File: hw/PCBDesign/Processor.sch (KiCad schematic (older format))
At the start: 26 parts, among them J4 Conn_ARM_JTAG_SWD_10, U11 74HC595, U12 74HC595, U13 STM32F446RETx, Y1 8MHz Crystal

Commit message: Lay out more PCB
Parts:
- added C29, C31, C33, C55, C56, C57: 100n, Capacitor_SMD:C_0402_1005Metric, symbol Device:C
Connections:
- net labels removed: BT_IRQ, BT_nPowerUp, BT_nWakeup, VSense_Analog, VSense_Radio, vBatt_Sense
- no-connect marks 6 -> 15
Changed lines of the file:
@@
 Text HLabel 8100 5700 2    50   Input ~ 0
 nBatt_Chg_Good
-Text HLabel 8800 1400 2    50   Input ~ 0
-vBatt_Sense
-Text HLabel 3350 2100 2    50   Output ~ 0
+Text HLabel 3550 2100 2    50   Output ~ 0
 nBattChgEn
-Text HLabel 3350 1900 2    50   Output ~ 0
+Text HLabel 3550 1900 2    50   Output ~ 0
 BattChgCfg0
-Text HLabel 3350 2000 2    50   Output ~ 0
+Text HLabel 3550 2000 2    50   Output ~ 0
 BattChgCfg1
 Text HLabel 7400 3700 0    50   Input ~ 0
@@
 Text HLabel 7400 3600 0    50   Output ~ 0
 BT_UART_TX
-Text HLabel 3350 2200 2    50   Output ~ 0
-BT_nWakeup
-Text HLabel 3350 2300 2    50   Output ~ 0
-BT_nPowerUp
-Text HLabel 7400 3800 0    50   Input ~ 0
-BT_IRQ
 Text HLabel 8800 2100 2    50   Output ~ 0
 RF24_MOSI
@@
 Text HLabel 8800 1500 2    50   Input ~ 0
 VSense_Digital
-Text HLabel 8800 1600 2    50   Input ~ 0
-VSense_Radio
-Text HLabel 8800 1700 2    50   Input ~ 0
-VSense_Analog
 Text HLabel 8100 1100 1    50   Input ~ 0
 V+
@@
 	6850 2700 6850 2600
 Connection ~ 6400 2700
-Text HLabel 3350 2400 2    50   Output ~ 0
+Text HLabel 3550 2400 2    50   Output ~ 0
 BT_VCC_EN
-Text HLabel 3350 2500 2    50   Output ~ 0
+Text HLabel 3550 2500 2    50   Output ~ 0
 RF24_VCC_EN
 Text Notes 3800 5600 0    50   ~ 0
@@
 Wire Wire Line
 	9400 2500 8800 2500
+NoConn ~ 7400 4300
+NoConn ~ 7400 4400
+NoConn ~ 7400 4500
+NoConn ~ 8800 3800
+NoConn ~ 8800 3300
+$Comp
+L Device:C C55
+U 1 1 6065388D
+P 5500 1300
+F 0 "C55" H 5615 1346 50  0000 L CNN
+F 1 "100n" H 5615 1255 50  0000 L CNN
+F 2 "Capacitor_SMD:C_0402_1005Metric" H 5538 1150 50  0001 C CNN
+F 3 "~" H 5500 1300 50  0001 C CNN
+F 4 "C1525" H 5500 1300 50  0001 C CNN "LCSC"
+	1    5500 1300
+	1    0    0    -1
+$EndComp
+$Comp
+L Device:C C56
+U 1 1 606541DA
+P 5900 1300
+F 0 "C56" H 6015 1346 50  0000 L CNN
+F 1 "100n" H 6015 1255 50  0000 L CNN
+F 2 "Capacitor_SMD:C_0402_1005Metric" H 5938 1150 50  0001 C CNN
+F 3 "~" H 5900 1300 50  0001 C CNN
+F 4 "C1525" H 5900 1300 50  0001 C CNN "LCSC"
+	1    5900 1300
+	1    0    0    -1
+$EndComp
+$Comp
+L Device:C C57
+U 1 1 6065440B
+P 6300 1300
+F 0 "C57" H 6415 1346 50  0000 L CNN
+F 1 "100n" H 6415 1255 50  0000 L CNN
+F 2 "Capacitor_SMD:C_0402_1005Metric" H 6338 1150 50  0001 C CNN
+F 3 "~" H 6300 1300 50  0001 C CNN
+F 4 "C1525" H 6300 1300 50  0001 C CNN "LCSC"
+	1    6300 1300
+	1    0    0    -1
+$EndComp
+$Comp
+L Device:C C33
+U 1 1 60654852
+P 5100 1300
+F 0 "C33" H 5215 1346 50  0000 L CNN
+F 1 "100n" H 5215 1255 50  0000 L CNN
+F 2 "Capacitor_SMD:C_0402_1005Metric" H 5138 1150 50  0001 C CNN
+F 3 "~" H 5100 1300 50  0001 C CNN
+F 4 "C1525" H 5100 1300 50  0001 C CNN "LCSC"
+	1    5100 1300
+	1    0    0    -1
+$EndComp
+$Comp
+L Device:C C31
+U 1 1 60654BAF
+P 4700 1300
+F 0 "C31" H 4815 1346 50  0000 L CNN
+F 1 "100n" H 4815 1255 50  0000 L CNN
+F 2 "Capacitor_SMD:C_0402_1005Metric" H 4738 1150 50  0001 C CNN
+F 3 "~" H 4700 1300 50  0001 C CNN
+F 4 "C1525" H 4700 1300 50  0001 C CNN "LCSC"
+	1    4700 1300
+	1    0    0    -1
+$EndComp
+$Comp
+L Device:C C29
+U 1 1 606550A4
+P 4300 1300
+F 0 "C29" H 4415 1346 50  0000 L CNN
+F 1 "100n" H 4415 1255 50  0000 L CNN
+F 2 "Capacitor_SMD:C_0402_1005Metric" H 4338 1150 50  0001 C CNN
+F 3 "~" H 4300 1300 50  0001 C CNN
+F 4 "C1525" H 4300 1300 50  0001 C CNN "LCSC"
+	1    4300 1300
+	1    0    0    -1
+$EndComp
+Text HLabel 5900 1150 1    50   Input ~ 0
+V+
+Text HLabel 5500 1150 1    50   Input ~ 0
+V+
+Text HLabel 5100 1150 1    50   Input ~ 0
+V+
+Text HLabel 4700 1150 1    50   Input ~ 0
+V+
+Text HLabel 4300 1150 1    50   Input ~ 0
+V+
+$Comp
+L power:GND #PWR0122
+U 1 1 60655583
+P 6300 1450
+F 0 "#PWR0122" H 6300 1200 50  0001 C CNN
+F 1 "GND" H 6305 1277 50  0000 C CNN
+F 2 "" H 6300 1450 50  0001 C CNN
+F 3 "" H 6300 1450 50  0001 C CNN
+	1    6300 1450
+	1    0    0    -1
+$EndComp
+$Comp
+L power:GND #PWR0123
+U 1 1 60655871
+P 5900 1450
+F 0 "#PWR0123" H 5900 1200 50  0001 C CNN
+F 1 "GND" H 5905 1277 50  0000 C CNN
+F 2 "" H 5900 1450 50  0001 C CNN
+F 3 "" H 5900 1450 50  0001 C CNN
+	1    5900 1450
+	1    0    0    -1
+$EndComp
+$Comp
+L power:GND #PWR0124
+U 1 1 606559F7
+P 5500 1450
+F 0 "#PWR0124" H 5500 1200 50  0001 C CNN
+F 1 "GND" H 5505 1277 50  0000 C CNN
+F 2 "" H 5500 1450 50  0001 C CNN
+F 3 "" H 5500 1450 50  0001 C CNN
+	1    5500 1450
+	1    0    0    -1
+$EndComp
+$Comp
+L power:GND #PWR0125
+U 1 1 60655C44
+P 5100 1450
+F 0 "#PWR0125" H 5100 1200 50  0001 C CNN
+F 1 "GND" H 5105 1277 50  0000 C CNN
+F 2 "" H 5100 1450 50  0001 C CNN
+F 3 "" H 5100 1450 50  0001 C CNN
+	1    5100 1450
+	1    0    0    -1
+$EndComp
+$Comp
+L power:GND #PWR0126
+U 1 1 60655DFB
+P 4700 1450
+F 0 "#PWR0126" H 4700 1200 50  0001 C CNN
+F 1 "GND" H 4705 1277 50  0000 C CNN
+F 2 "" H 4700 1450 50  0001 C CNN
+F 3 "" H 4700 1450 50  0001 C CNN
+	1    4700 1450
+	1    0    0    -1
+$EndComp
+$Comp
+L power:GND #PWR0127
+U 1 1 6065602B
+P 4300 1450
+F 0 "#PWR0127" H 4300 1200 50  0001 C CNN
+F 1 "GND" H 4305 1277 50  0000 C CNN
+F 2 "" H 4300 1450 50  0001 C CNN
+F 3 "" H 4300 1450 50  0001 C CNN
+	1    4300 1450
+	1    0    0    -1
+$EndComp
+Text HLabel 6300 1150 1    50   Input ~ 0
+VDDA
+NoConn ~ 7400 3800
+NoConn ~ 8800 1400
+NoConn ~ 8800 1600
+NoConn ~ 8800 1700
 $EndSCHEMATC

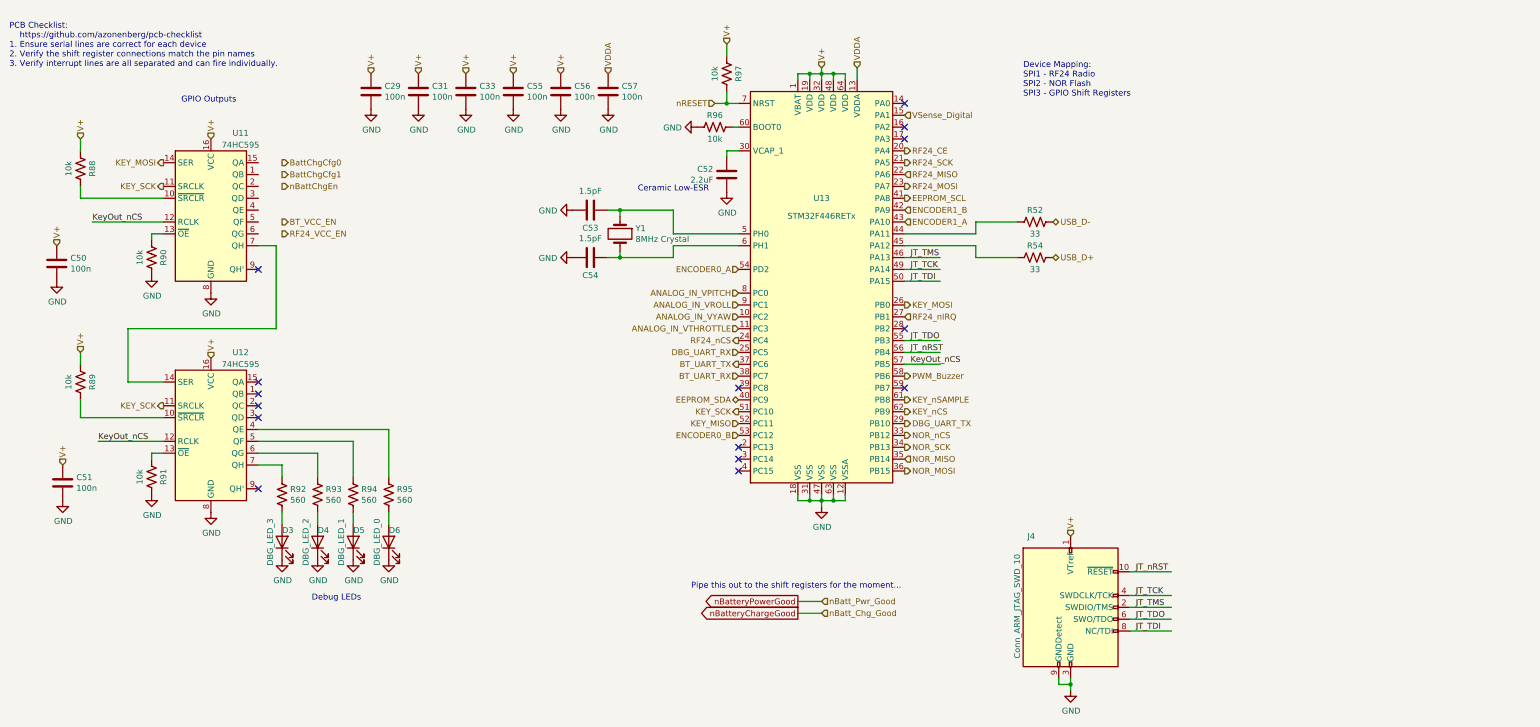
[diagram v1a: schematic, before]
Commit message: Routed most of the core peripherals
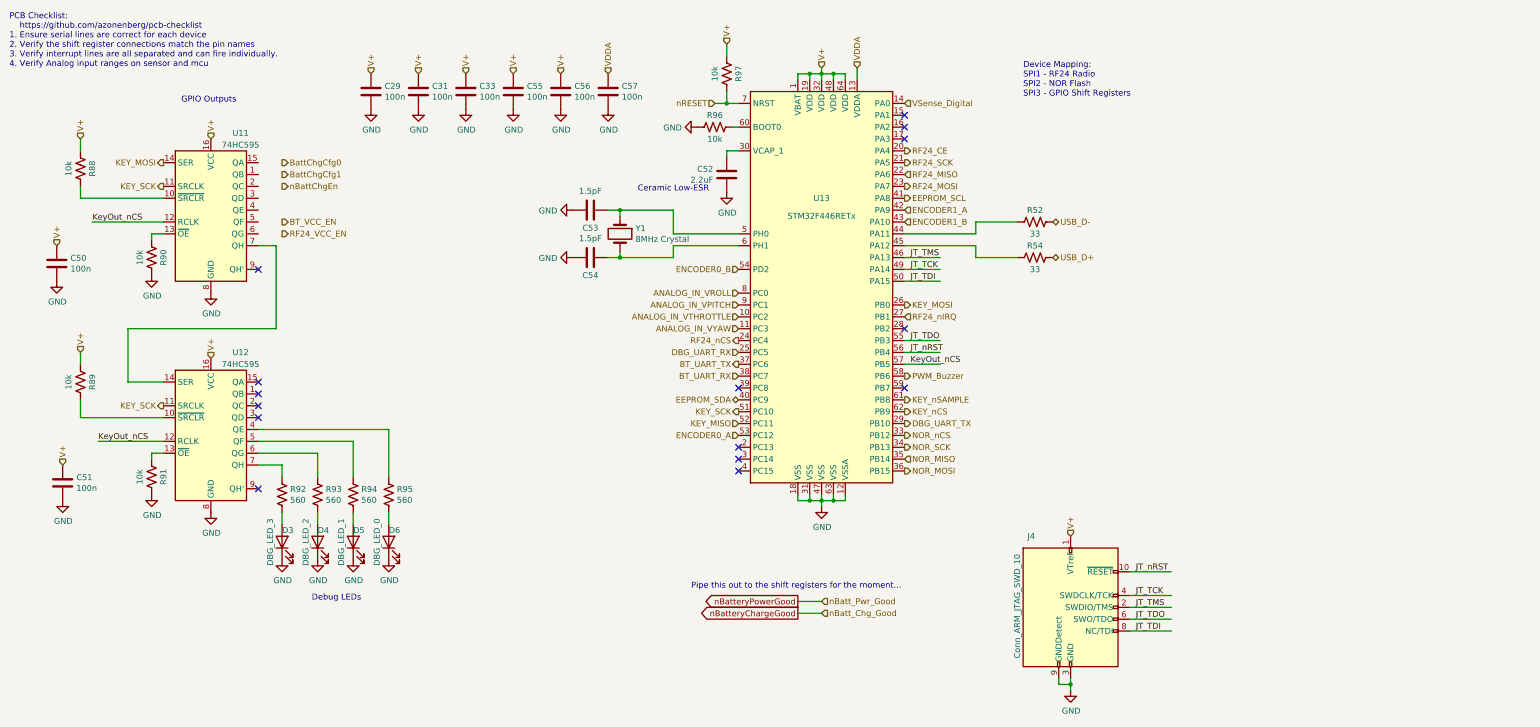
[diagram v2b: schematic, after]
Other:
- note added: "PCB Checklist: \n https://github.com/azonenberg/pcb-checklist\n1. Ensure serial lines are correct for each device\n2. Verify the shift register connections match the pin names\n3. Verify interrupt lines are all separated and can fire individually.\n4. Verify Analog input ranges on sensor and mcu"
- note removed: "PCB Checklist: \n https://github.com/azonenberg/pcb-checklist\n1. Ensure serial lines are correct for each device\n2. Verify the shift register connections match the pin names\n3. Verify interrupt lines are all separated and can fire individually."
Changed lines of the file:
@@
 Text HLabel 8800 2200 2    50   Output ~ 0
 EEPROM_SCL
-Text HLabel 8800 1500 2    50   Input ~ 0
+Text HLabel 8800 1400 2    50   Input ~ 0
 VSense_Digital
 Text HLabel 8100 1100 1    50   Input ~ 0
@@
 Text HLabel 8800 3900 2    50   Output ~ 0
 KEY_nSAMPLE
+Text HLabel 7400 4200 0    50   Input ~ 0
+ENCODER0_A
 Text HLabel 7400 2800 0    50   Input ~ 0
-ENCODER0_A
-Text HLabel 7400 4200 0    50   Input ~ 0
 ENCODER0_B
+Text HLabel 8800 2300 2    50   Input ~ 0
+ENCODER1_A
 Text HLabel 8800 2400 2    50   Input ~ 0
-ENCODER1_A
-Text HLabel 8800 2300 2    50   Input ~ 0
 ENCODER1_B
+Text HLabel 7400 3100 0    50   Input ~ 0
+ANALOG_IN_VPITCH
 Text HLabel 7400 3000 0    50   Input ~ 0
-ANALOG_IN_VPITCH
-Text HLabel 7400 3100 0    50   Input ~ 0
 ANALOG_IN_VROLL
+Text HLabel 7400 3300 0    50   Input ~ 0
+ANALOG_IN_VYAW
 Text HLabel 7400 3200 0    50   Input ~ 0
-ANALOG_IN_VYAW
-Text HLabel 7400 3300 0    50   Input ~ 0
 ANALOG_IN_VTHROTTLE
 Wire Wire Line
@@
 DBG_UART_RX
 Text Notes 1250 1100 0    50   ~ 0
-PCB Checklist: \n    https://github.com/azonenberg/pcb-checklist\n1. Ensure serial lines are correct for each device\n2. Verify the shift register connections match the pin names\n3. Verify interrupt lines are all separated and can fire individually.
+PCB Checklist: \n    https://github.com/azonenberg/pcb-checklist\n1. Ensure serial lines are correct for each device\n2. Verify the shift register connections match the pin names\n3. Verify interrupt lines are all separated and can fire individually.\n4. Verify Analog input ranges on sensor and mcu
 Text Notes 9800 1350 0    50   ~ 0
 Device Mapping:\nSPI1 - RF24 Radio\nSPI2 - NOR Flash\nSPI3 - GPIO Shift Registers
@@
 VDDA
 NoConn ~ 7400 3800
-NoConn ~ 8800 1400
 NoConn ~ 8800 1600
 NoConn ~ 8800 1700
+NoConn ~ 8800 1500
 $EndSCHEMATC

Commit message: Complete route of draft #1 finished
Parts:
- removed C51: 100n, Capacitor_SMD:C_0402_1005Metric, symbol Device:C
- removed D3: DBG_LED_3, LED_SMD:LED_0603_1608Metric, symbol Device:LED
- removed R89, R91: 10k, Resistor_SMD:R_0402_1005Metric, symbol Device:R_US
- removed R92: 560, Resistor_SMD:R_0402_1005Metric, symbol Device:R_US
- removed U12: 74HC595, Package_SO:SO-16_3.9x9.9mm_P1.27mm, symbol 74xx:74HC595
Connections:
- wire segments 90 -> 76
- no-connect marks 15 -> 10
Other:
- moved on the sheet: D4, D5, D6, R93, R94, R95

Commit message: Finished preliminary route of PCB after design review checklist
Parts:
- added D3: STATUS_LED, LED_SMD:LED_0603_1608Metric, symbol Device:LED
- added R65, R89, R91: 10k, Resistor_SMD:R_0402_1005Metric, symbol Device:R_US
- added R92: 560, Resistor_SMD:R_0402_1005Metric, symbol Device:R_US
- added TP15, TP16, TP17, TP18, TP19, TP20, TP21, TP22: TestPoint, TestPoint:TestPoint_Pad_2.5x2.5mm, symbol Connector:TestPoint
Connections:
- wire segments 76 -> 82
- no-connect marks 10 -> 9
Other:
- note removed: "PCB Checklist: \n https://github.com/azonenberg/pcb-checklist\n1. Ensure serial lines are correct for each device\n2. Verify the shift register connections match the pin names\n3. Verify interrupt lines are all separated and can fire individually.\n4. Verify Analog input ranges on sensor and mcu"
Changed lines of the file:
@@
 Text HLabel 8800 2200 2    50   Output ~ 0
 EEPROM_SCL
-Text HLabel 8800 1400 2    50   Input ~ 0
+Text HLabel 9100 1400 2    50   Input ~ 0
 VSense_Digital
 Text HLabel 8100 1100 1    50   Input ~ 0
@@
 Text HLabel 7400 4200 0    50   Input ~ 0
 ENCODER0_A
-Text HLabel 7400 2800 0    50   Input ~ 0
+Text HLabel 7400 4300 0    50   Input ~ 0
 ENCODER0_B
 Text HLabel 8800 2300 2    50   Input ~ 0
@@
 Text Label 8850 2700 0    50   ~ 0
 JT_TMS
-Text HLabel 8800 4100 2    50   Output ~ 0
+Text HLabel 10050 4100 2    50   Output ~ 0
 DBG_UART_TX
-Text HLabel 7400 3500 0    50   Input ~ 0
+Text HLabel 6150 3500 0    50   Input ~ 0
 DBG_UART_RX
-Text Notes 1250 1100 0    50   ~ 0
-PCB Checklist: \n    https://github.com/azonenberg/pcb-checklist\n1. Ensure serial lines are correct for each device\n2. Verify the shift register connections match the pin names\n3. Verify interrupt lines are all separated and can fire individually.\n4. Verify Analog input ranges on sensor and mcu
 Text Notes 9800 1350 0    50   ~ 0
 Device Mapping:\nSPI1 - RF24 Radio\nSPI2 - NOR Flash\nSPI3 - GPIO Shift Registers
@@
 Wire Wire Line
 	9400 2500 8800 2500
-NoConn ~ 7400 4300
 NoConn ~ 7400 4400
 NoConn ~ 7400 4500
@@
 Text HLabel 6300 1150 1    50   Input ~ 0
 VDDA
-NoConn ~ 7400 3800
 NoConn ~ 8800 1600
 NoConn ~ 8800 1700
 NoConn ~ 8800 1500
+$Comp
+L Device:R_US R65
+U 1 1 605A69C7
+P 8950 1400
+F 0 "R65" V 8850 1400 50  0000 C CNN
+F 1 "10k" V 9050 1400 50  0000 C CNN
+F 2 "Resistor_SMD:R_0402_1005Metric" V 8990 1390 50  0001 C CNN
+F 3 "~" H 8950 1400 50  0001 C CNN
+F 4 "C25744" H 8950 1400 50  0001 C CNN "LCSC"
+	1    8950 1400
+	0    1    1    0
+$EndComp
+$Comp
+L Device:R_US R91
+U 1 1 605B2DF4
+P 9900 4100
+F 0 "R91" V 9800 4100 50  0000 C CNN
+F 1 "10k" V 10000 4100 50  0000 C CNN
+F 2 "Resistor_SMD:R_0402_1005Metric" V 9940 4090 50  0001 C CNN
+F 3 "~" H 9900 4100 50  0001 C CNN
+F 4 "C25744" H 9900 4100 50  0001 C CNN "LCSC"
+	1    9900 4100
+	0    1    1    0
+$EndComp
+Wire Wire Line
+	9750 4100 8800 4100
+$Comp
+L Device:R_US R89
+U 1 1 605B77B2
+P 6300 3500
+F 0 "R89" V 6200 3500 50  0000 C CNN
+F 1 "10k" V 6400 3500 50  0000 C CNN
+F 2 "Resistor_SMD:R_0402_1005Metric" V 6340 3490 50  0001 C CNN
+F 3 "~" H 6300 3500 50  0001 C CNN
+F 4 "C25744" H 6300 3500 50  0001 C CNN "LCSC"
+	1    6300 3500
+	0    1    1    0
+$EndComp
+NoConn ~ 7400 2800
+Wire Wire Line
+	6450 3500 7400 3500
+$Comp
+L Connector:TestPoint TP?
+U 1 1 605CFE2B
+P 3500 5500
+AR Path="/6045890B/605CFE2B" Ref="TP?"  Part="1"
+AR Path="/604707FB/605CFE2B" Ref="TP18"  Part="1"
+F 0 "TP18" H 3558 5618 50  0000 L CNN
+F 1 "TestPoint" H 3558 5527 50  0000 L CNN
+F 2 "TestPoint:TestPoint_Pad_2.5x2.5mm" H 3700 5500 50  0001 C CNN
+F 3 "~" H 3700 5500 50  0001 C CNN
+	1    3500 5500
+	1    0    0    -1
+$EndComp
+$Comp
+L power:GND #PWR09
+U 1 1 605D1BD5
+P 3500 5500
+F 0 "#PWR09" H 3500 5250 50  0001 C CNN
+F 1 "GND" H 3505 5327 50  0000 C CNN
+F 2 "" H 3500 5500 50  0001 C CNN
+F 3 "" H 3500 5500 50  0001 C CNN
+	1    3500 5500
+	1    0    0    -1
+$EndComp
+$Comp
+L Connector:TestPoint TP?
+U 1 1 605D1DEB
+P 4000 5500
+AR Path="/6045890B/605D1DEB" Ref="TP?"  Part="1"
+AR Path="/604707FB/605D1DEB" Ref="TP15"  Part="1"
+F 0 "TP15" H 4058 5618 50  0000 L CNN
+F 1 "TestPoint" H 4058 5527 50  0000 L CNN
+F 2 "TestPoint:TestPoint_Pad_2.5x2.5mm" H 4200 5500 50  0001 C CNN
+F 3 "~" H 4200 5500 50  0001 C CNN
+	1    4000 5500
+	1    0    0    -1
+$EndComp
+$Comp
+L Connector:TestPoint TP?
+U 1 1 605D20E0
+P 4500 5500
+AR Path="/6045890B/605D20E0" Ref="TP?"  Part="1"
+AR Path="/604707FB/605D20E0" Ref="TP16"  Part="1"
+F 0 "TP16" H 4558 5618 50  0000 L CNN
+F 1 "TestPoint" H 4558 5527 50  0000 L CNN
+F 2 "TestPoint:TestPoint_Pad_2.5x2.5mm" H 4700 5500 50  0001 C CNN
+F 3 "~" H 4700 5500 50  0001 C CNN
+	1    4500 5500
+	1    0    0    -1
+$EndComp
+$Comp
+L Connector:TestPoint TP?
+U 1 1 605D227A
+P 5000 5500
+AR Path="/6045890B/605D227A" Ref="TP?"  Part="1"
+AR Path="/604707FB/605D227A" Ref="TP17"  Part="1"
+F 0 "TP17" H 5058 5618 50  0000 L CNN
+F 1 "TestPoint" H 5058 5527 50  0000 L CNN
+F 2 "TestPoint:TestPoint_Pad_2.5x2.5mm" H 5200 5500 50  0001 C CNN
+F 3 "~" H 5200 5500 50  0001 C CNN
+	1    5000 5500
+	1    0    0    -1
+$EndComp
+$Comp
+L Connector:TestPoint TP?
+U 1 1 605D23A2
+P 5500 5500
+AR Path="/6045890B/605D23A2" Ref="TP?"  Part="1"
+AR Path="/604707FB/605D23A2" Ref="TP19"  Part="1"
+F 0 "TP19" H 5558 5618 50  0000 L CNN
+F 1 "TestPoint" H 5558 5527 50  0000 L CNN
+F 2 "TestPoint:TestPoint_Pad_2.5x2.5mm" H 5700 5500 50  0001 C CNN
+F 3 "~" H 5700 5500 50  0001 C CNN
+	1    5500 5500
+	1    0    0    -1
+$EndComp
+Text HLabel 4500 5500 3    50   Output ~ 0
+KEY_MOSI
+Text HLabel 5000 5500 3    50   Input ~ 0
+KEY_MISO
+Text HLabel 4000 5500 3    50   Output ~ 0
+KEY_SCK
+Text Label 5500 5500 3    50   ~ 0
+KeyOut_nCS
+Wire Wire Line
+	5500 5500 5500 5800
+$Comp
+L Connector:TestPoint TP?
+U 1 1 605D756E
+P 6000 5500
+AR Path="/6045890B/605D756E" Ref="TP?"  Part="1"
+AR Path="/604707FB/605D756E" Ref="TP20"  Part="1"
+F 0 "TP20" H 6058 5618 50  0000 L CNN
+F 1 "TestPoint" H 6058 5527 50  0000 L CNN
+F 2 "TestPoint:TestPoint_Pad_2.5x2.5mm" H 6200 5500 50  0001 C CNN
+F 3 "~" H 6200 5500 50  0001 C CNN
+	1    6000 5500
+	1    0    0    -1
+$EndComp
+Text HLabel 6000 5500 3    50   Output ~ 0
+KEY_nSAMPLE
+$Comp
+L Connector:TestPoint TP?
+U 1 1 605D9B3F
+P 6500 5500
+AR Path="/6045890B/605D9B3F" Ref="TP?"  Part="1"
+AR Path="/604707FB/605D9B3F" Ref="TP21"  Part="1"
+F 0 "TP21" H 6558 5618 50  0000 L CNN
+F 1 "TestPoint" H 6558 5527 50  0000 L CNN
+F 2 "TestPoint:TestPoint_Pad_2.5x2.5mm" H 6700 5500 50  0001 C CNN
+F 3 "~" H 6700 5500 50  0001 C CNN
+	1    6500 5500
+	1    0    0    -1
+$EndComp
+Text HLabel 6500 5500 3    50   Output ~ 0
+KEY_nCS
+$Comp
+L Connector:TestPoint TP?
+U 1 1 605E052A
+P 6150 3150
+AR Path="/6045890B/605E052A" Ref="TP?"  Part="1"
+AR Path="/604707FB/605E052A" Ref="TP22"  Part="1"
+F 0 "TP22" H 6208 3268 50  0000 L CNN
+F 1 "TestPoint" H 6208 3177 50  0000 L CNN
+F 2 "TestPoint:TestPoint_Pad_2.5x2.5mm" H 6350 3150 50  0001 C CNN
+F 3 "~" H 6350 3150 50  0001 C CNN
+	1    6150 3150
+	1    0    0    -1
+$EndComp
+$Comp
+L power:GND #PWR012
+U 1 1 605E0530
+P 6150 3150
+F 0 "#PWR012" H 6150 2900 50  0001 C CNN
+F 1 "GND" H 6155 2977 50  0000 C CNN
+F 2 "" H 6150 3150 50  0001 C CNN
+F 3 "" H 6150 3150 50  0001 C CNN
+	1    6150 3150
+	1    0    0    -1
+$EndComp
+$Comp
+L Device:LED D3
+U 1 1 6066A05B
+P 6400 4550
+F 0 "D3" V 6500 4550 50  0000 R CNN
+F 1 "STATUS_LED" H 6600 4650 50  0000 R CNN
+F 2 "LED_SMD:LED_0603_1608Metric" H 6400 4550 50  0001 C CNN
+F 3 "~" H 6400 4550 50  0001 C CNN
+F 4 "C72041" H 6400 4550 50  0001 C CNN "LCSC"
+	1    6400 4550
+	0    -1   -1   0
+$EndComp
+$Comp
+L power:GND #PWR090
+U 1 1 6066A061
+P 6400 4700
+F 0 "#PWR090" H 6400 4450 50  0001 C CNN
+F 1 "GND" H 6405 4527 50  0000 C CNN
+F 2 "" H 6400 4700 50  0001 C CNN
+F 3 "" H 6400 4700 50  0001 C CNN
+	1    6400 4700
+	1    0    0    -1
+$EndComp
+Wire Wire Line
+	6400 4300 6400 4400
+$Comp
+L Device:R_US R92
+U 1 1 6066A054
+P 6400 4150
+F 0 "R92" H 6332 4104 50  0000 R CNN
+F 1 "560" H 6332 4195 50  0000 R CNN
+F 2 "Resistor_SMD:R_0402_1005Metric" V 6440 4140 50  0001 C CNN
+F 3 "~" H 6400 4150 50  0001 C CNN
+F 4 "C11702" H 6400 4150 50  0001 C CNN "LCSC"
+	1    6400 4150
+	-1   0    0    1
+$EndComp
+Wire Wire Line
+	7400 3800 6400 3800
+Wire Wire Line
+	6400 3800 6400 4000
 $EndSCHEMATC

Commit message: Adjust components for lowest build cost
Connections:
- net labels added: VSense_Batt
- net labels removed: BattChgCfg0, BattChgCfg1, VSense_Digital
- no-connect marks 9 -> 11
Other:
- note removed: "Device Mapping:\nSPI1 - RF24 Radio\nSPI2 - NOR Flash\nSPI3 - GPIO Shift Registers"
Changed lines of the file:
@@
 Text HLabel 3350 2300 2    50   Output ~ 0
 nBattChgEn
-Text HLabel 3350 2100 2    50   Output ~ 0
-BattChgCfg0
-Text HLabel 3350 2200 2    50   Output ~ 0
-BattChgCfg1
 Text HLabel 7400 3700 0    50   Input ~ 0
 BT_UART_RX
@@
 EEPROM_SCL
 Text HLabel 9100 1400 2    50   Input ~ 0
-VSense_Digital
+VSense_Batt
 Text HLabel 8100 1100 1    50   Input ~ 0
 V+
@@
 Text HLabel 6150 3500 0    50   Input ~ 0
 DBG_UART_RX
-Text Notes 9800 1350 0    50   ~ 0
-Device Mapping:\nSPI1 - RF24 Radio\nSPI2 - NOR Flash\nSPI3 - GPIO Shift Registers
 Text GLabel 7900 5600 0    50   Output ~ 0
 nBatteryPowerGood
@@
 Wire Wire Line
 	6400 3800 6400 4000
+NoConn ~ 3350 2200
+NoConn ~ 3350 2100
 $EndSCHEMATC
